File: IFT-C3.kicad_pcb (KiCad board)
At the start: 2 copper layers, 54 x 85.6 mm, 73 parts, among them IC1 DIO5508XS8, J1 Conn_01x04_Socket, J2 Conn_01x10_Pin, J3 USB4085-GF-A_REVB, J4 Conn_01x10_Pin, J5 SJ-3523-SMT-TR, J6 Conn_01x02_Pin, J7 Conn_01x02, Q1 Q_Photo_NPN, Q2 Q_NMOS_GSD, SW1 SW_Push_Dual, SW10 SW_Push_Dual, SW3 SW_Push_Dual, SW4 SW_Push_Dual, SW5 SW_Push_Dual, SW6 SW_Push_Dual, SW7 SW_Push_Dual, SW8 SW_Push_Dual, SW9 SW_Push_Dual, U1 AZ1117CR-3.3TRG1, U2 ESP32-C3-WROOM-02

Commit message: Uniformed values for R and C for a better BOM
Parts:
- C10, C5, C8: value 100nF -> 100n
- C6, C7: value 10uF -> 10u
- R14: value 10k -> 10K
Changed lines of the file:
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@@
 		)
 		(property ki_fp_filters "LED* LED_SMD:* LED_THT:*")
-		(sheetname "Racine")
+		(sheetname "Root")
 		(sheetfile "IFT-C3.kicad_sch")
 		(attr smd)
@@
 			)
 		)
-		(sheetname "Racine")
+		(sheetname "Root")
 		(sheetfile "IFT-C3.kicad_sch")
 		(attr through_hole)
@@
 			)
 		)
-		(property "Value" "10uF"
+		(property "Value" "10u"
 			(at 0 1.679999 90)
 			(layer "F.Fab")
@@
 		)
 		(property ki_fp_filters "C_*")
-		(sheetname "Racine")
+		(sheetname "Root")
 		(sheetfile "IFT-C3.kicad_sch")
 		(attr smd)
@@
 		)
 		(property ki_fp_filters "LED*IN-PI554FCH*PLCC*5.0x5.0mm*P3.2mm*")
-		(sheetname "Racine")
+		(sheetname "Root")
 		(sheetfile "IFT-C3.kicad_sch")
 		(attr smd)
@@
 		)
 		(property ki_fp_filters "Connector*:*_1x??_*")
-		(sheetname "Racine")
+		(sheetname "Root")
 		(sheetfile "IFT-C3.kicad_sch")
 		(attr through_hole)
@@
 		)
 		(property ki_fp_filters "LED* LED_SMD:* LED_THT:*")
-		(sheetname "Racine")
+		(sheetname "Root")
 		(sheetfile "IFT-C3.kicad_sch")
 		(attr smd)
@@
 		)
 		(property ki_fp_filters "R_*")
-		(sheetname "Racine")
+		(sheetname "Root")
 		(sheetfile "IFT-C3.kicad_sch")
 		(attr smd)
@@
 		)
 		(property ki_fp_filters "SolderJumper*Open*")
-		(sheetname "Racine")
+		(sheetname "Root")
 		(sheetfile "IFT-C3.kicad_sch")
 		(attr exclude_from_pos_files)
@@
 		)
 		(property ki_fp_filters "R_*")
-		(sheetname "Racine")
+		(sheetname "Root")
 		(sheetfile "IFT-C3.kicad_sch")
 		(attr smd)
@@
 		)
 		(property ki_fp_filters "Inductor_* L_* *Ferrite*")
-		(sheetname "Racine")
+		(sheetname "Root")
 		(sheetfile "IFT-C3.kicad_sch")
 		(attr smd)
@@
 		)
 		(property ki_fp_filters "Connector*:*_1x??_*")
-		(sheetname "Racine")
+		(sheetname "Root")
 		(sheetfile "IFT-C3.kicad_sch")
 		(attr smd)
@@
 		)
 		(property ki_fp_filters "SolderJumper*Open*")
-		(sheetname "Racine")
+		(sheetname "Root")
 		(sheetfile "IFT-C3.kicad_sch")
 		(attr exclude_from_pos_files)
@@
 		)
 		(property ki_fp_filters "R_*")
-		(sheetname "Racine")
+		(sheetname "Root")
 		(sheetfile "IFT-C3.kicad_sch")
 		(attr smd)
@@
 			)
 		)
-		(sheetname "Racine")
+		(sheetname "Root")
 		(sheetfile "IFT-C3.kicad_sch")
 		(attr smd)
@@
 			)
 		)
-		(property "Value" "10uF"
+		(property "Value" "10u"
 			(at 0 -1.679999 90)
 			(layer "B.Fab")
@@
 		)
 		(property ki_fp_filters "C_*")
-		(sheetname "Racine")
+		(sheetname "Root")
 		(sheetfile "IFT-C3.kicad_sch")
 		(attr smd)
@@
 		)
 		(property ki_fp_filters "R_*")
-		(sheetname "Racine")
+		(sheetname "Root")
 		(sheetfile "IFT-C3.kicad_sch")
 		(attr smd)
@@
 		)
 		(property ki_fp_filters "C_*")
-		(sheetname "Racine")
+		(sheetname "Root")
 		(sheetfile "IFT-C3.kicad_sch")
 		(attr smd)
@@
 		(tags "capacitor handsolder")
 		(property "Reference" "C5"
-			(at 0 -1.700001 360)
+			(at 0 -1.700001 0)
 			(layer "B.SilkS")
 			(effects
@@
 			)
 		)
-		(property "Value" "100nF"
-			(at 0 -1.679999 360)
+		(property "Value" "100n"
+			(at 0 -1.679999 0)
 			(layer "B.Fab")
 			(effects
@@
 		)
 		(property ki_fp_filters "C_*")
-		(sheetname "Racine")
+		(sheetname "Root")
 		(sheetfile "IFT-C3.kicad_sch")
 		(attr smd)
@@
 		)
 		(fp_text user "${REFERENCE}"
-			(at 0 0 360)
+			(at 0 0 0)
 			(layer "B.Fab")
 			(effects
@@
 		)
 		(property ki_fp_filters "R_*")
-		(sheetname "Racine")
+		(sheetname "Root")
 		(sheetfile "IFT-C3.kicad_sch")
 		(attr smd)
@@
 		)
 		(property ki_fp_filters "SolderJumper*Open*")
-		(sheetname "Racine")
+		(sheetname "Root")
 		(sheetfile "IFT-C3.kicad_sch")
 		(attr exclude_from_pos_files)
@@
 		)
 		(property ki_fp_filters "R_*")
-		(sheetname "Racine")
+		(sheetname "Root")
 		(sheetfile "IFT-C3.kicad_sch")
 		(attr smd)
@@
 			)
 		)
-		(sheetname "Racine")
+		(sheetname "Root")
 		(sheetfile "IFT-C3.kicad_sch")
 		(attr smd)
@@
 			)
 		)
-		(sheetname "Racine")
+		(sheetname "Root")
 		(sheetfile "IFT-C3.kicad_sch")
 		(attr smd)
@@
 		)
 		(property ki_fp_filters "R_*")
-		(sheetname "Racine")
+		(sheetname "Root")
 		(sheetfile "IFT-C3.kicad_sch")
 		(attr smd)
@@
 		)
 		(property ki_fp_filters "SolderJumper*Open*")
-		(sheetname "Racine")
+		(sheetname "Root")
 		(sheetfile "IFT-C3.kicad_sch")
 		(attr exclude_from_pos_files)
@@
 			)
 		)
-		(property "Value" "100nF"
+		(property "Value" "100n"
 			(at 0 -1.68 90)
 			(layer "B.Fab")
@@
 		)
 		(property ki_fp_filters "LED*IN-PI554FCH*PLCC*5.0x5.0mm*P3.2mm*")
-		(sheetname "Racine")
+		(sheetname "Root")
 		(sheetfile "IFT-C3.kicad_sch")
 		(attr smd)
@@
 		)
 		(property ki_fp_filters "Connector*:*_1x??_*")
-		(sheetname "Racine")
+		(sheetname "Root")
 		(sheetfile "IFT-C3.kicad_sch")
 		(attr through_hole)
@@
 		)
 		(property ki_fp_filters "SOT?223* SOT?89* TO?220* TO?252* TO?263*")
-		(sheetname "Racine")
+		(sheetname "Root")
 		(sheetfile "IFT-C3.kicad_sch")
 		(attr smd)
@@
 			)
 		)
-		(property "Value" "100nF"
+		(property "Value" "100n"
 			(at 0 -1.68 90)
 			(layer "B.Fab")
@@
 		)
 		(property ki_fp_filters "SolderJumper*Open*")
-		(sheetname "Racine")
+		(sheetname "Root")
 		(sheetfile "IFT-C3.kicad_sch")
 		(attr exclude_from_pos_files)
@@
 		)
 		(property ki_fp_filters "Connector*:*_1x??_*")
-		(sheetname "Racine")
+		(sheetname "Root")
 		(sheetfile "IFT-C3.kicad_sch")
 		(attr through_hole)
@@
 		)
 		(property ki_fp_filters "C_*")
-		(sheetname "Racine")
+		(sheetname "Root")
 		(sheetfile "IFT-C3.kicad_sch")
 		(attr smd)
@@
 		)
 		(property ki_fp_filters "R_*")
-		(sheetname "Racine")
+		(sheetname "Root")
 		(sheetfile "IFT-C3.kicad_sch")
 		(attr smd)
@@
 		)
 		(property ki_fp_filters "R_*")
-		(sheetname "Racine")
+		(sheetname "Root")
 		(sheetfile "IFT-C3.kicad_sch")
 		(attr smd)
@@
 			)
 		)
-		(sheetname "Racine")
+		(sheetname "Root")
 		(sheetfile "IFT-C3.kicad_sch")
 		(attr through_hole)
@@
 		)
 		(property ki_fp_filters "Connector*:*_1x??_*")
-		(sheetname "Racine")
+		(sheetname "Root")
 		(sheetfile "IFT-C3.kicad_sch")
 		(attr through_hole)
@@
 		)
 		(property ki_fp_filters "C_*")
-		(sheetname "Racine")
+		(sheetname "Root")
 		(sheetfile "IFT-C3.kicad_sch")
 		(attr smd)
@@
 		)
 		(property ki_fp_filters "R_*")
-		(sheetname "Racine")
+		(sheetname "Root")
 		(sheetfile "IFT-C3.kicad_sch")
 		(attr smd)
@@
 			)
 		)
-		(sheetname "Racine")
+		(sheetname "Root")
 		(sheetfile "IFT-C3.kicad_sch")
 		(attr through_hole)
@@
 			)
 		)
-		(sheetname "Racine")
+		(sheetname "Root")
 		(sheetfile "IFT-C3.kicad_sch")
 		(attr through_hole)
@@
 		)
 		(property ki_fp_filters "SolderJumper*Open*")
-		(sheetname "Racine")
+		(sheetname "Root")
 		(sheetfile "IFT-C3.kicad_sch")
 		(attr exclude_from_pos_files)
@@
 			)
 		)
-		(property "Value" "10k"
+		(property "Value" "10K"
 			(at 0 -1.65 0)
 			(layer "B.Fab")
@@
 		)
 		(property ki_fp_filters "R_*")
-		(sheetname "Racine")
+		(sheetname "Root")
 		(sheetfile "IFT-C3.kicad_sch")
 		(attr smd)
@@
 		)
 		(property ki_fp_filters "SolderJumper*Open*")
-		(sheetname "Racine")
+		(sheetname "Root")
 		(sheetfile "IFT-C3.kicad_sch")
 		(zone_connect 1)
@@
 		)
 		(property ki_fp_filters "C_*")
-		(sheetname "Racine")
+		(sheetname "Root")
 		(sheetfile "IFT-C3.kicad_sch")
 		(attr smd)
@@
 			)
 		)
-		(sheetname "Racine")
+		(sheetname "Root")
 		(sheetfile "IFT-C3.kicad_sch")
 		(attr smd)

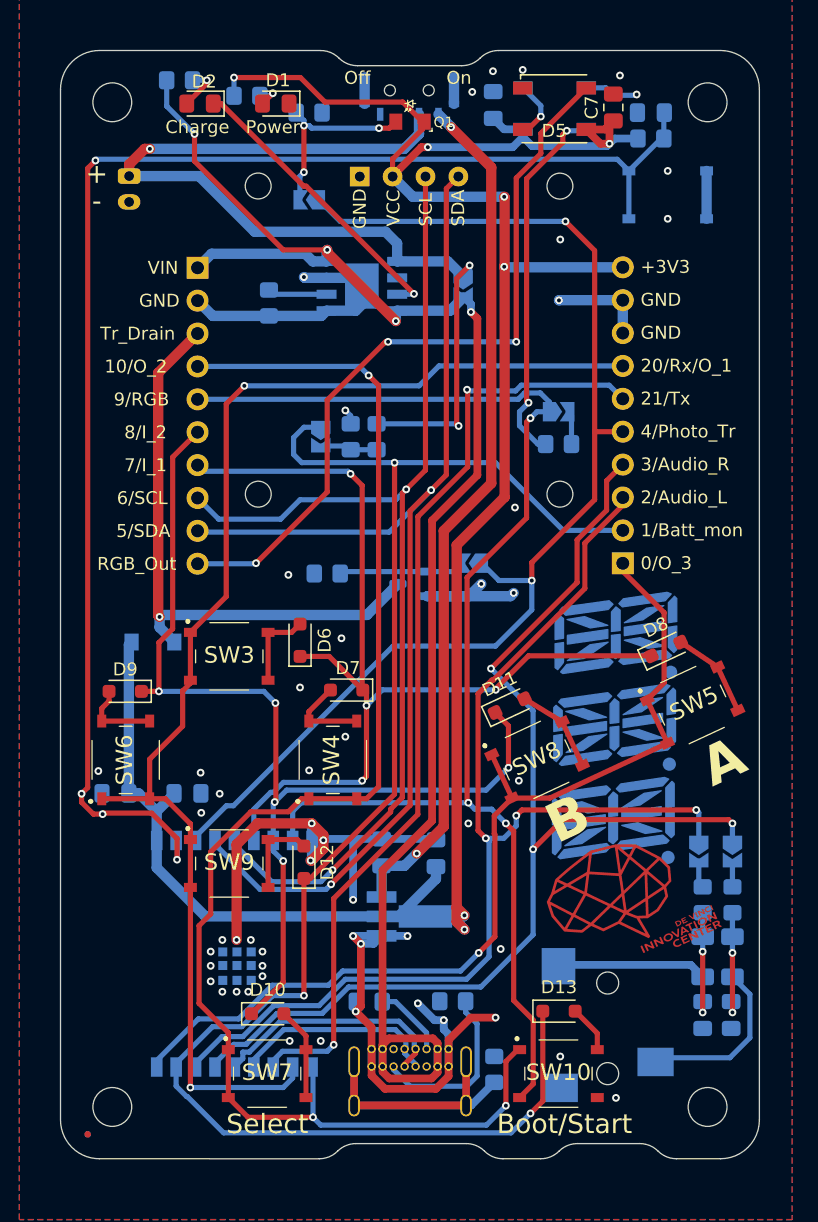
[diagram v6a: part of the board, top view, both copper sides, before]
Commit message: Bugs fixed (buttons and OLED holes)
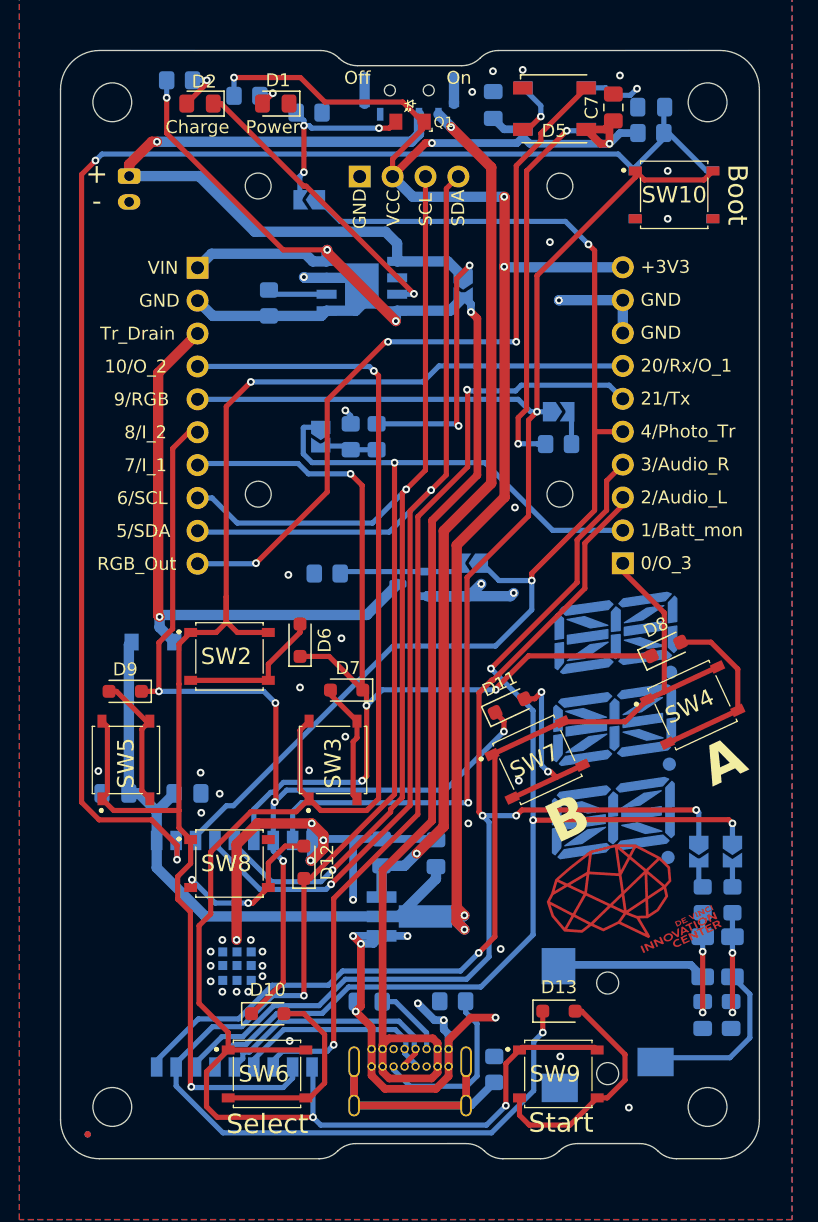
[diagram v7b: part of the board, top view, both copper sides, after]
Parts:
- added SW2: PTS526_SK15_SMTR2_LFS, footprints:PTS526SK15SMTR2LFS, F.Cu at (39.1, 77.8)
- S3: footprint Local footprints:MSK12C02 -> footprints:MSK12C02
- SW1, SW10, SW3, SW4, SW5, SW6, SW7, SW8, SW9: value SW_Push_Dual -> PTS526_SK15_SMTR2_LFS; footprint footprints:PTS526SM15SMTR2LFS -> footprints:PTS526SK15SMTR2LFS
- moved SW10 68.5 mm to (73.4, 42.1)
- moved SW5 44.0 mm to (31.1, 85.8), turned to 90 degrees
- moved SW7 32.0 mm to (62.9, 85.8), turned to 25 degrees
- moved SW9 30.2 mm to (64.5, 110.0)
- moved SW4 28.1 mm to (74.9, 81.5), turned to 25 degrees
- moved SW6 26.6 mm to (42.0, 110.0), turned to 0 degrees
- moved SW8 25.1 mm to (39.1, 93.8), turned to 0 degrees
- moved SW3 11.3 mm to (47.1, 85.8), turned to 90 degrees
- moved SW1 0.48 mm to (73.4, 42.1)
- moved C3 0.43 mm to (71.7, 35.3)
- moved R3 0.43 mm to (71.6, 37.3)
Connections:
- SW1 pad 1: GND -> Net-(U2-EN/CHIP_PU)
- SW1 pad 4: Net-(U2-EN/CHIP_PU) -> GND
- SW10 pad 1: O_2 -> RGB_LEDs
- SW10 pad 2: Net-(D13-A) -> RGB_LEDs
- SW10 pad 3: RGB_LEDs -> GND
- SW3 pad 1: O_1 -> O_2
- SW3 pad 2: Net-(D6-A) -> O_2
- SW3 pad 3: O_1 -> Net-(D7-A)
- SW3 pad 4: Net-(D6-A) -> Net-(D7-A)
- SW4 pad 1: O_2 -> O_3
- SW4 pad 2: Net-(D7-A) -> O_3
- SW4 pad 3: O_2 -> Net-(D8-A)
- SW4 pad 4: Net-(D7-A) -> Net-(D8-A)
- SW5 pad 1: O_3 -> O_1
- SW5 pad 2: Net-(D8-A) -> O_1
- SW5 pad 3: O_3 -> Net-(D9-A)
- SW5 pad 4: Net-(D8-A) -> Net-(D9-A)
- SW6 pad 1: O_1 -> O_2
- SW6 pad 2: Net-(D9-A) -> O_2
- SW6 pad 3: O_1 -> Net-(D10-A)
- SW6 pad 4: Net-(D9-A) -> Net-(D10-A)
- SW7 pad 1: O_2 -> O_3
- SW7 pad 2: Net-(D10-A) -> O_3
- SW7 pad 3: O_2 -> Net-(D11-A)
- SW7 pad 4: Net-(D10-A) -> Net-(D11-A)
- SW8 pad 1: O_3 -> O_1
- SW8 pad 2: Net-(D11-A) -> O_1
- SW8 pad 3: O_3 -> Net-(D12-A)
- SW8 pad 4: Net-(D11-A) -> Net-(D12-A)
- SW9 pad 1: O_1 -> O_2
- SW9 pad 2: Net-(D12-A) -> O_2
- SW9 pad 3: O_1 -> Net-(D13-A)
- SW9 pad 4: Net-(D12-A) -> Net-(D13-A)
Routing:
- net O_2: track 112.6 -> 135.8 mm
- net Net-(D13-A): track 3.68 -> 18.5 mm
- net O_1: track 101.9 -> 115.6 mm
- net Net-(D10-A): track 7.18 -> 15.5 mm
- net Net-(D11-A): track 7.12 -> 14.7 mm, vias 0 -> 2
- net Net-(D8-A): track 7.13 -> 14.5 mm
- net Net-(D12-A): track 6.68 -> 13.0 mm, vias 0 -> 2
- net Net-(D6-A): track 6.43 -> 11.4 mm
- net Net-(D9-A): track 6.23 -> 10.6 mm
- net GND: track 126.6 -> 123.1 mm, vias 53 -> 52
- net Net-(D7-A): track 6.79 -> 9.50 mm
- net Net-(U2-EN/CHIP_PU): track 112.8 -> 115.2 mm, vias 4 -> 2
- net Batt_mon: track 127.5 -> 125.6 mm
- net I_2: track 81.3 -> 79.5 mm
- net Audio_L: track 87.1 -> 86.1 mm
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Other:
- board text added: "Boot"
- board text added: "Start"
- board text removed: "Boot/Start"

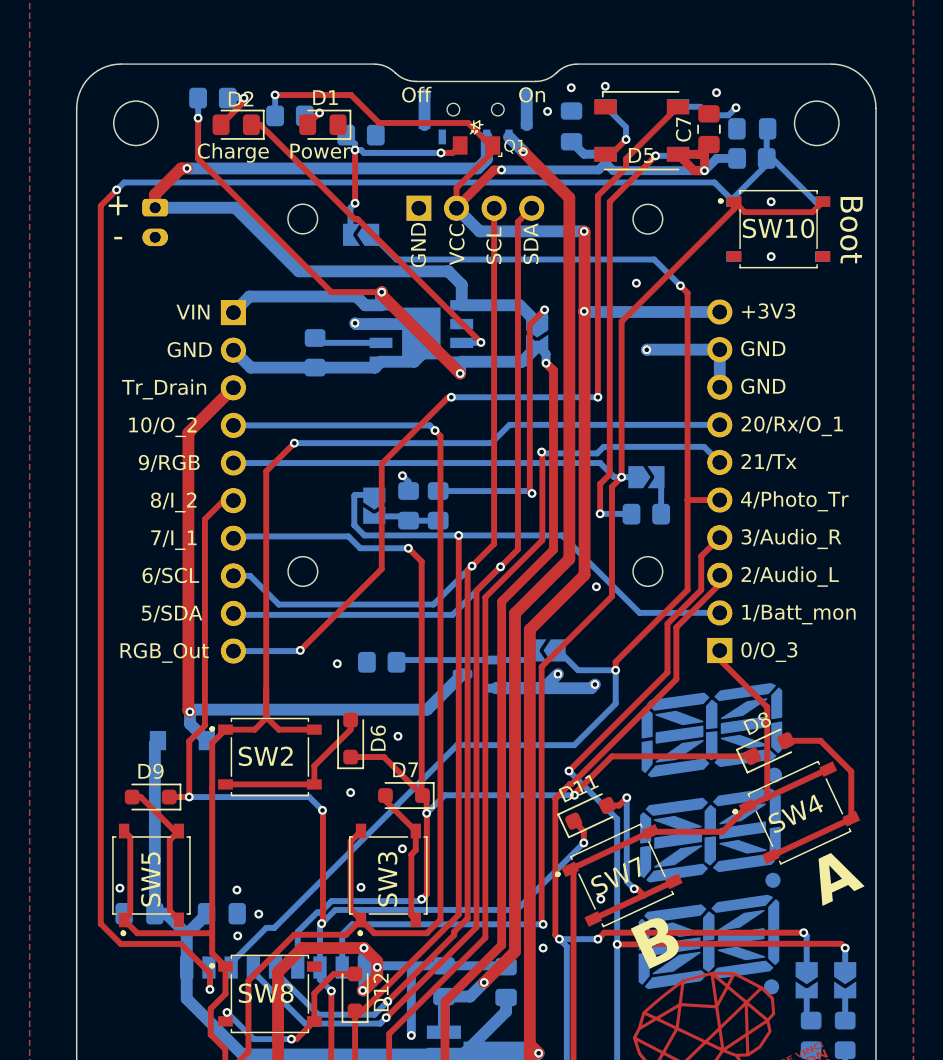
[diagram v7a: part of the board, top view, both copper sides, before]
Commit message: Buttons fixed, boot buuton added, footprint of the switch should be easier to solder by hand
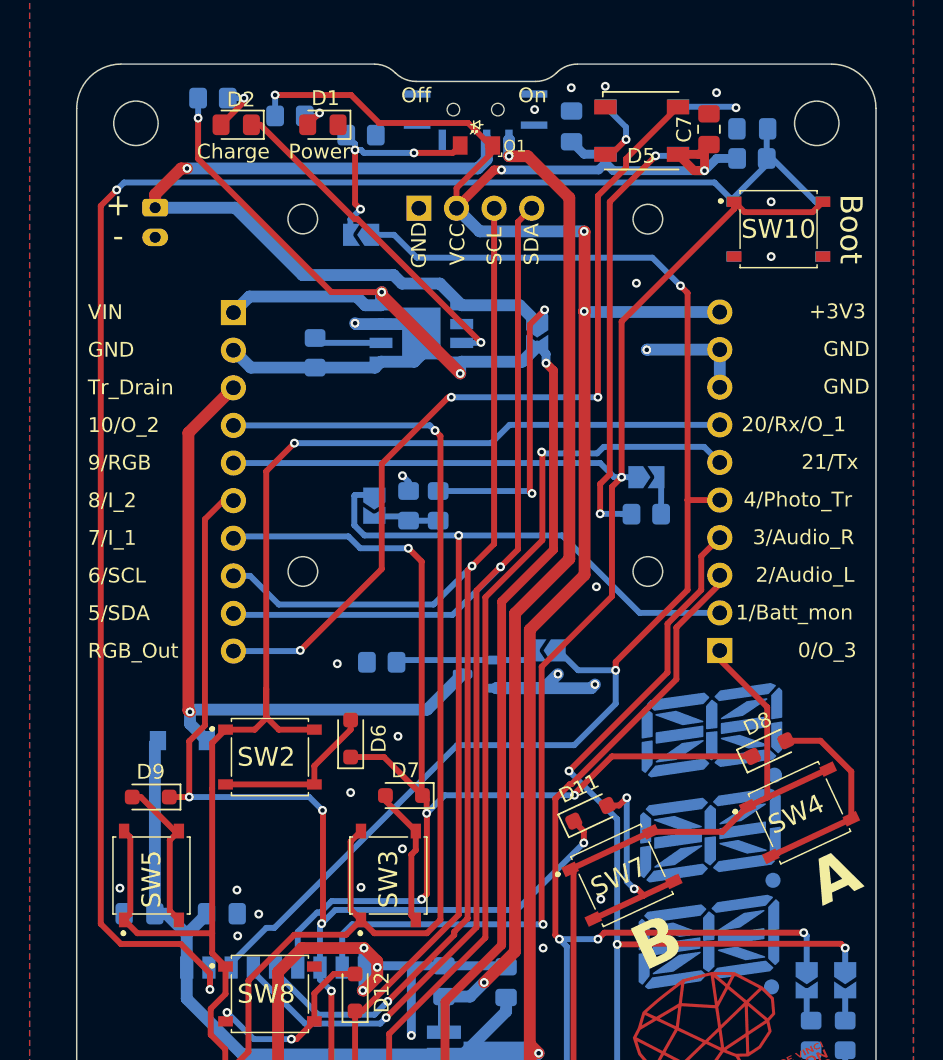
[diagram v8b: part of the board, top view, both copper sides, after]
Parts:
- J2, J4: footprint Connector_PinHeader_2.54mm:PinHeader_1x10_P2.54mm_Horizontal -> Connector_PinHeader_2.54mm:PinHeader_1x10_P2.54mm_Vertical
- R5: value 10K -> 1K
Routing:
- net GND: track 123.1 -> 118.6 mm
- net +BATT: track 76.0 -> 75.0 mm
- net +BATT_after_switch: track 66.7 -> 67.2 mm
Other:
- board text added: "v2024.1"
- board text removed: "v2024"
